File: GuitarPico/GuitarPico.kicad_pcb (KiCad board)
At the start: 2 copper layers, 100 x 100 mm, 132 parts, among them J1 INPUT, J2 INPUT, J3 OUTPUT, J4 OUTPUT, J5 Barrel_Jack_Switch, J6 VGA, J8 INPUT, J9 INPUT, Q1 2N3904, Q2 2N3904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

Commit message: Minor code fixes
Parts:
- moved C7 0.28 mm to (85.1, 72.3)
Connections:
- J2 pad G: unconnected-(J2-PadG) -> GND
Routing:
- net Net-(R7-Pad1): track 39.3 -> 42.2 mm
- net Net-(C7-Pad1): track 16.4 -> 17.0 mm

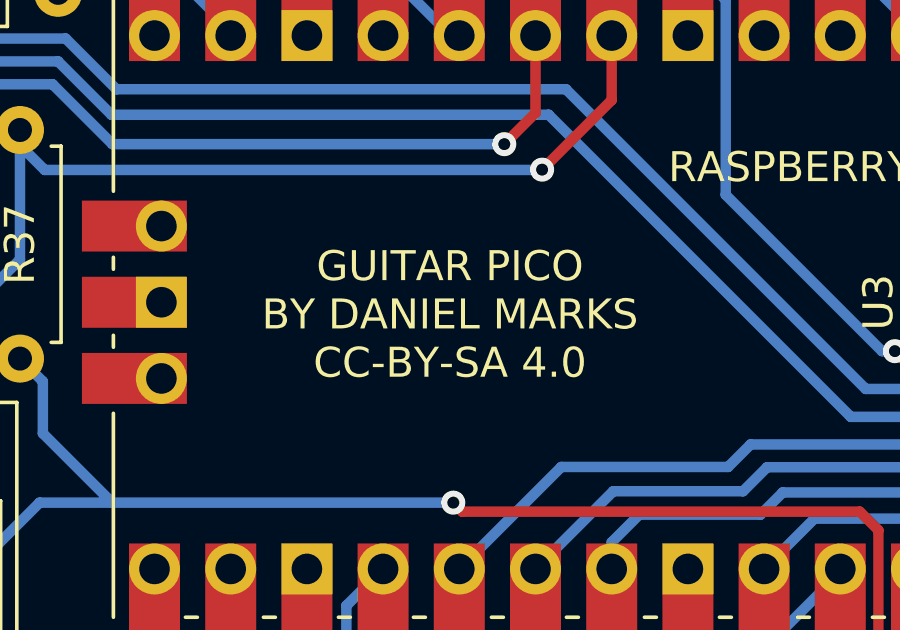
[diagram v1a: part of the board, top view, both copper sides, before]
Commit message: Refactored dsp structures into two parts
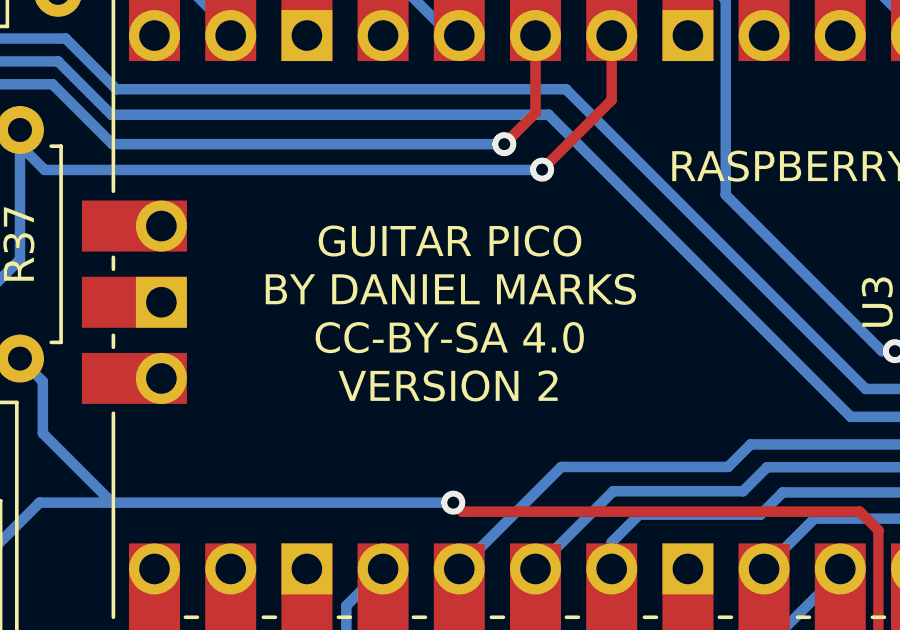
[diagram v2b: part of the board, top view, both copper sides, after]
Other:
- board text added: "GUITAR PICO BY DANIEL MARKS CC-BY-SA 4.0 VERSION 2"
- board text removed: "GUITAR PICO BY DANIEL MARKS CC-BY-SA 4.0"
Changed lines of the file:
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@@
     (effects (font (size 1 1) (thickness 0.15)))
   )
-  (gr_text "GUITAR PICO\nBY DANIEL MARKS\nCC-BY-SA 4.0" (at 101.97 113.91) (layer "F.SilkS")
+  (gr_text "GUITAR PICO\nBY DANIEL MARKS\nCC-BY-SA 4.0\nVERSION 2" (at 101.97 113.91) (layer "F.SilkS")
     (effects (font (size 1 1) (thickness 0.15)))
   )
